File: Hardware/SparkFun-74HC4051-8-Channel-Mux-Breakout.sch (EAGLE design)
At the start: 12 parts, among them U1 74HC4051BQ

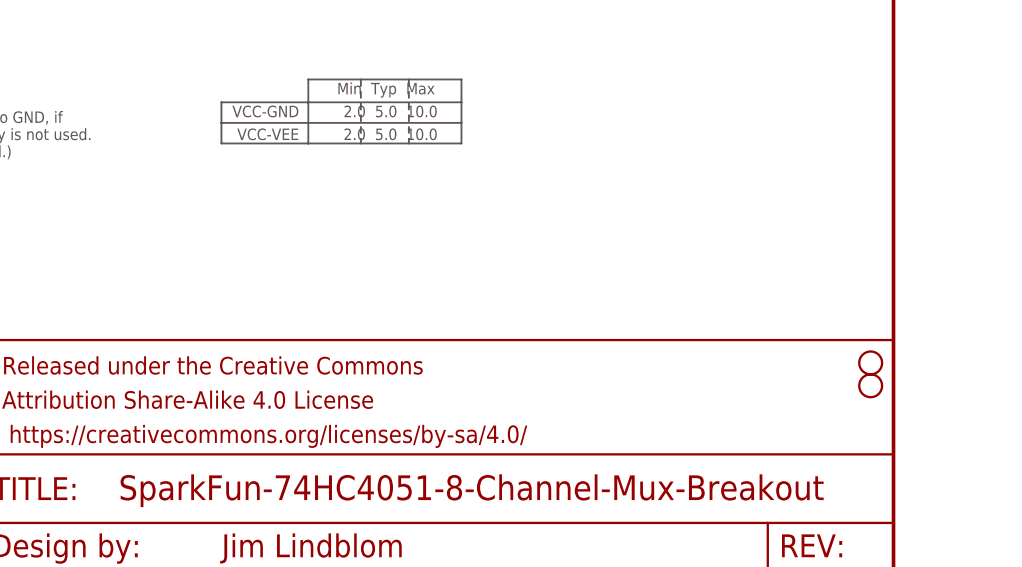
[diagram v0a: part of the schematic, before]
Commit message: Resolving issues flagged on issue 1.
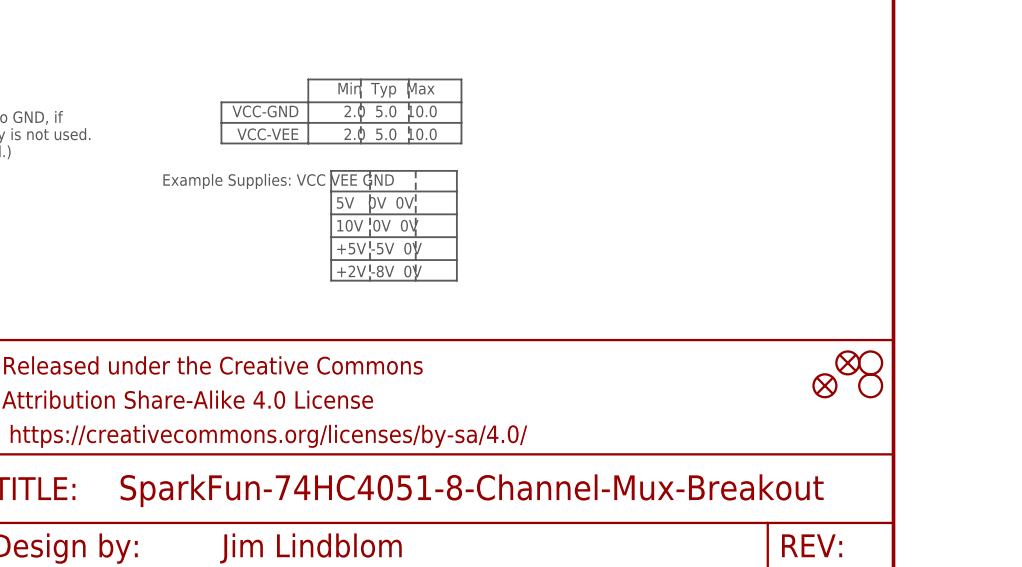
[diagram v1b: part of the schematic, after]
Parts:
- added FD1, FD2: FIDUCIAL1X2, SparkFun-Aesthetics:FIDUCIAL1X2
- J1: device SparkFun-Connectors:M111X11_NO_SILK -> SparkFun-Connectors:M11PTH
- J2: device SparkFun-Connectors:M08NO_SILK -> SparkFun-Connectors:M08
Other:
- note added: "+2V -8V 0V"
- note added: "+5V -5V 0V"
- note added: "10V 0V 0V"
- note added: "5V 0V 0V"
- note added: "Example Supplies: VCC VEE GND"
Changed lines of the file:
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@@
 <part name="SUPPLY1" library="SparkFun-Aesthetics" deviceset="VCC" device=""/>
 <part name="GND1" library="SparkFun-Aesthetics" deviceset="GND" device=""/>
-<part name="J1" library="SparkFun-Connectors" deviceset="M11" device="1X11_NO_SILK"/>
+<part name="J1" library="SparkFun-Connectors" deviceset="M11" device="PTH"/>
 <part name="SUPPLY2" library="SparkFun-Aesthetics" deviceset="VCC" device=""/>
 <part name="GND2" library="SparkFun-Aesthetics" deviceset="GND" device=""/>
 <part name="GND3" library="SparkFun-Aesthetics" deviceset="GND" device=""/>
 <part name="SUPPLY3" library="SparkFun-Aesthetics" deviceset="VCC" device=""/>
-<part name="J2" library="SparkFun-Connectors" deviceset="M08" device="NO_SILK"/>
+<part name="J2" library="SparkFun-Connectors" deviceset="M08" device=""/>
 <part name="GND4" library="SparkFun-Aesthetics" deviceset="GND" device=""/>
 <part name="SUPPLY4" library="SparkFun-Aesthetics" deviceset="VCC" device=""/>
@@
 <part name="JP1" library="SparkFun-Passives" deviceset="JUMPER-PAD-2-NC_BY_PASTE" device="NO-SILK" value="VEE-GND"/>
 <part name="GND6" library="SparkFun-Aesthetics" deviceset="GND" device=""/>
+<part name="FD1" library="SparkFun-Aesthetics" deviceset="FIDUCIAL" device="1X2"/>
+<part name="FD2" library="SparkFun-Aesthetics" deviceset="FIDUCIAL" device="1X2"/>
 </parts>
 <sheets>
@@
 (low). Pull !E! directly to
 VCC to disable the mux.</text>
+<text x="167.64" y="53.34" size="1.27" layer="97" font="vector" align="center-left">Example Supplies: VCC VEE GND</text>
+<text x="186.944" y="48.26" size="1.27" layer="97" font="vector" align="center-left">10V  0V  0V</text>
+<text x="186.944" y="45.72" size="1.27" layer="97" font="vector" align="center-left">+5V -5V  0V</text>
+<text x="186.944" y="43.18" size="1.27" layer="97" font="vector" align="center-left">+2V -8V  0V</text>
+<text x="186.944" y="50.8" size="1.27" layer="97" font="vector" align="center-left">5V   0V  0V</text>
+<wire x1="186.436" y1="42.164" x2="186.436" y2="44.45" width="0.2032" layer="97"/>
+<wire x1="186.436" y1="44.45" x2="186.436" y2="46.99" width="0.2032" layer="97"/>
+<wire x1="186.436" y1="46.99" x2="186.436" y2="49.53" width="0.2032" layer="97"/>
+<wire x1="186.436" y1="49.53" x2="186.436" y2="52.07" width="0.2032" layer="97"/>
+<wire x1="186.436" y1="52.07" x2="186.436" y2="54.356" width="0.2032" layer="97"/>
+<wire x1="200.406" y1="42.164" x2="195.834" y2="42.164" width="0.2032" layer="97"/>
+<wire x1="195.834" y1="42.164" x2="190.754" y2="42.164" width="0.2032" layer="97"/>
+<wire x1="190.754" y1="42.164" x2="186.436" y2="42.164" width="0.2032" layer="97"/>
+<wire x1="200.406" y1="42.164" x2="200.406" y2="44.45" width="0.2032" layer="97"/>
+<wire x1="200.406" y1="44.45" x2="200.406" y2="46.99" width="0.2032" layer="97"/>
+<wire x1="200.406" y1="46.99" x2="200.406" y2="49.53" width="0.2032" layer="97"/>
+<wire x1="200.406" y1="49.53" x2="200.406" y2="52.07" width="0.2032" layer="97"/>
+<wire x1="200.406" y1="52.07" x2="200.406" y2="54.356" width="0.2032" layer="97"/>
+<wire x1="200.406" y1="54.356" x2="195.834" y2="54.356" width="0.2032" layer="97"/>
+<wire x1="195.834" y1="54.356" x2="190.754" y2="54.356" width="0.2032" layer="97"/>
+<wire x1="190.754" y1="54.356" x2="186.436" y2="54.356" width="0.2032" layer="97"/>
+<wire x1="190.754" y1="54.356" x2="190.754" y2="42.164" width="0.2032" layer="97" style="shortdash"/>
+<wire x1="195.834" y1="54.356" x2="195.834" y2="42.164" width="0.2032" layer="97" style="shortdash"/>
+<wire x1="186.436" y1="52.07" x2="200.406" y2="52.07" width="0.2032" layer="97"/>
+<wire x1="186.436" y1="49.53" x2="200.406" y2="49.53" width="0.2032" layer="97"/>
+<wire x1="186.436" y1="46.99" x2="200.406" y2="46.99" width="0.2032" layer="97"/>
+<wire x1="186.436" y1="44.45" x2="200.406" y2="44.45" width="0.2032" layer="97"/>
 </plain>
 <instances>
@@
 <instance part="JP1" gate="G$1" x="129.54" y="58.42" rot="R90"/>
 <instance part="GND6" gate="1" x="129.54" y="48.26"/>
+<instance part="FD1" gate="G$1" x="243.84" y="33.02"/>
+<instance part="FD2" gate="G$1" x="241.3" y="30.48"/>
 </instances>
 <busses>

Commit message: Fixing silkscreen, upping to v10
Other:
- note added: "Example Supplies"
- note added: "VCC VEE GND"
- note added: "v10"
- note removed: "Example Supplies: VCC VEE GND"
- note removed: "v01"

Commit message: Swapping 100k resistor out with 10k
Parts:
- R1: value 100k -> 10k; device SparkFun-Resistors:100KOHM-0603-1/10W-1% -> SparkFun-Resistors:10KOHM-0603-1/10W-1%
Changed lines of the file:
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@@
 <setting verticaltext="up"/>
 </settings>
-<grid distance="0.05" unitdist="inch" unit="inch" style="lines" multiple="1" display="no" altdistance="0.01" altunitdist="inch" altunit="inch"/>
+<grid distance="0.1" unitdist="inch" unit="inch" style="lines" multiple="1" display="no" altdistance="0.01" altunitdist="inch" altunit="inch"/>
 <layers>
 <layer number="1" name="Top" color="4" fill="1" visible="no" active="no"/>
@@
 <part name="GND4" library="SparkFun-Aesthetics" deviceset="GND" device=""/>
 <part name="SUPPLY4" library="SparkFun-Aesthetics" deviceset="VCC" device=""/>
-<part name="R1" library="SparkFun-Resistors" deviceset="100KOHM" device="-0603-1/10W-1%" value="100k"/>
+<part name="R1" library="SparkFun-Resistors" deviceset="10KOHM" device="-0603-1/10W-1%" value="10k"/>
 <part name="H1" library="SparkFun-Electromechanical" deviceset="STAND-OFF" device=""/>
 <part name="H2" library="SparkFun-Electromechanical" deviceset="STAND-OFF" device=""/>

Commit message: Schematic cleanup.
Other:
- note added: "VCC/VEE/GND Range"
